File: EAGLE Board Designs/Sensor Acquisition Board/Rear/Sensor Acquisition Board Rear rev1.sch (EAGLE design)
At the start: 26 parts, among them J10 JUMPER_0603_, J4 CONNECTOR-SENSOR_NF_S_RA_BLACK, J5 CONNECTOR-SENSOR_NF_S_RA_BLACK, J6 CONNECTOR-SENSOR_NF_S_RA_BLACK, J7 CONNECTOR-SENSOR_NF_S_RA_BLACK, J9 CONNECTOR-CAN_NF_S_RA_BLACK, U1 VOLTAGE_REGULATOR_SOT-223_5V, U3 TCAN1051HQV-Q1

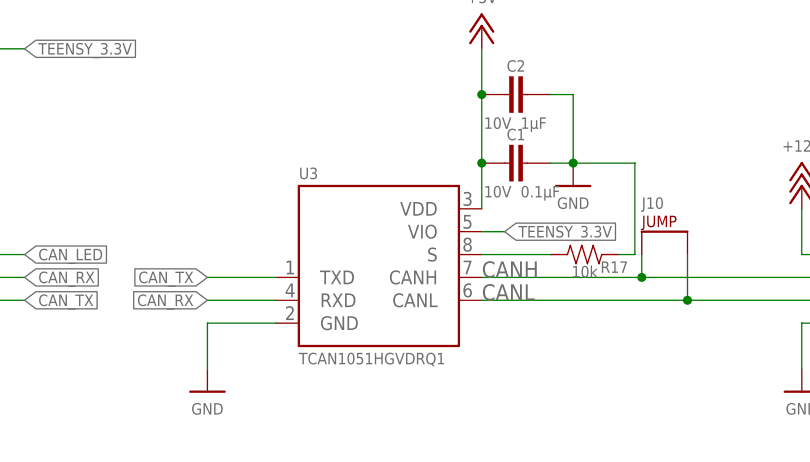
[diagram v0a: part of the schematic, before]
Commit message: TCAN to MCP on rear
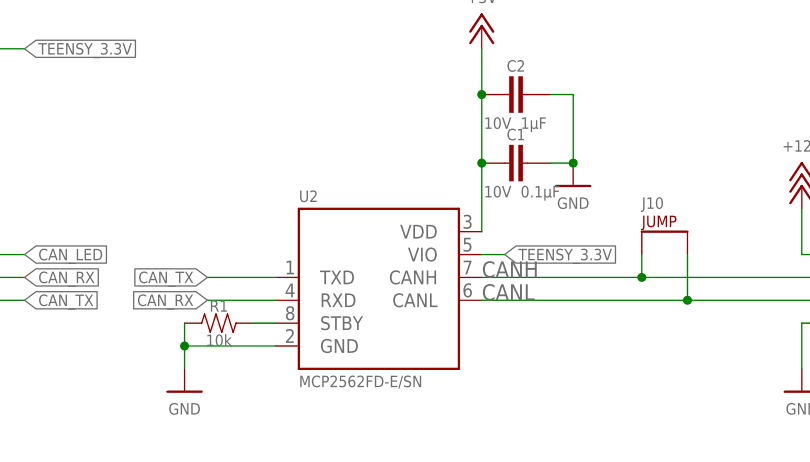
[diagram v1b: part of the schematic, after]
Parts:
- removed R17: RESISTOR_0603_10K, HyTechDevices:RESISTOR_0603_10K
- removed U3: TCAN1051HQV-Q1, HyTechDevices:TCAN1051HQV-Q1
- added R1: RESISTOR_0603_10K, HyTechDevices:RESISTOR_0603_10K
- added U2: MCP2562FD, HyTechDevices:MCP2562FD
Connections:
- removed net N$4: R17.1, U3.S
- new net N$3: R1.2, U2.STBY
- net +5V: now also U2.VDD; no longer U3.VDD
- net CANH: now also U2.CANH; no longer U3.CANH
- net CANL: now also U2.CANL; no longer U3.CANL
- net CAN_RX: now also U2.RXD; no longer U3.RXD
- net CAN_TX: now also U2.TXD; no longer U3.TXD
- net GND: now also R1.1, U2.GND; no longer R17.2, U3.GND
- net TEENSY_3.3V: now also U2.VIO; no longer U3.VIO
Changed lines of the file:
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@@
 <part name="P1" library="HyTechSupplies" deviceset="+5V" device=""/>
 <part name="P2" library="HyTechSupplies" deviceset="GND" device=""/>
-<part name="U3" library="HyTechDevices" deviceset="TCAN1051*V-Q1" device="" technology="HQ"/>
 <part name="C1" library="HyTechDevices" deviceset="CAPACITOR_?_*" device="0603" technology="10V_0.1UF"/>
 <part name="GND1" library="HyTechSupplies" deviceset="GND" device=""/>
@@
 <part name="P9" library="HyTechSupplies" deviceset="GND" device=""/>
 <part name="P10" library="HyTechSupplies" deviceset="+5V" device=""/>
-<part name="R17" library="HyTechDevices" deviceset="RESISTOR_?_*" device="0603" technology="10K"/>
 <part name="J6" library="HyTechDevices" deviceset="CONNECTOR-SENSOR_?_*" device="NF_S_RA" technology="BLACK"/>
 <part name="J5" library="HyTechDevices" deviceset="CONNECTOR-SENSOR_?_*" device="NF_S_RA" technology="BLACK"/>
@@
 <part name="R14" library="HyTechDevices" deviceset="RESISTOR_?_*" device="0603" technology="12K" value="RESISTOR_0603_12K"/>
 <part name="A2" library="HyTechDevices" deviceset="TEENSY_4.0" device=""/>
+<part name="U2" library="HyTechDevices" deviceset="MCP2562FD" device=""/>
+<part name="R1" library="HyTechDevices" deviceset="RESISTOR_?_*" device="0603" technology="10K"/>
 </parts>
 <sheets>
@@
 <attribute name="VALUE" x="114.3" y="95.25" size="1.27" layer="96" align="top-center"/>
 </instance>
-<instance part="U3" gate="G$1" x="182.88" y="121.92" smashed="yes">
-<attribute name="NAME" x="182.88" y="122.682" size="1.27" layer="95"/>
-<attribute name="MPN" x="182.88" y="103.378" size="1.27" layer="95" align="top-left"/>
-</instance>
 <instance part="C1" gate="G$1" x="208.28" y="124.46" smashed="yes">
 <attribute name="NAME" x="207.01" y="127" size="1.27" layer="95" align="bottom-center"/>
@@
 <attribute name="CAPACITANCE" x="207.518" y="129.54" size="1.27" layer="96" align="top-left"/>
 </instance>
-<instance part="P3" gate="1" x="172.72" y="99.06" smashed="yes">
-<attribute name="VALUE" x="172.72" y="97.79" size="1.27" layer="96" align="top-center"/>
+<instance part="P3" gate="1" x="170.18" y="99.06" smashed="yes">
+<attribute name="VALUE" x="170.18" y="97.79" size="1.27" layer="96" align="top-center"/>
 </instance>
 <instance part="J9" gate="G$1" x="254" y="116.84" smashed="yes" rot="MR0">
@@
 <attribute name="VALUE" x="43.18" y="129.54" size="1.27" layer="96" align="bottom-center"/>
 </instance>
-<instance part="R17" gate="G$1" x="215.9" y="114.3" smashed="yes">
-<attribute name="NAME" x="217.932" y="112.268" size="1.27" layer="95" align="bottom-center"/>
-<attribute name="RESISTANCE" x="214.63" y="113.03" size="1.27" layer="96" align="top-center"/>
-</instance>
 <instance part="J6" gate="G$1" x="215.9" y="200.66" smashed="yes" rot="MR0">
 <attribute name="NAME" x="215.9" y="201.295" size="1.27" layer="95" rot="MR0"/>
@@
 </instance>
 <instance part="A2" gate="G$1" x="121.92" y="144.78" smashed="yes"/>
+<instance part="U2" gate="G$1" x="182.88" y="119.38" smashed="yes">
+<attribute name="NAME" x="182.88" y="120.142" size="1.27" layer="95"/>
+<attribute name="MPN" x="182.88" y="100.838" size="1.27" layer="95" align="top-left"/>
+</instance>
+<instance part="R1" gate="G$1" x="175.26" y="106.68" smashed="yes">
+<attribute name="NAME" x="173.99" y="107.95" size="1.27" layer="95" align="bottom-center"/>
+<attribute name="RESISTANCE" x="173.99" y="105.41" size="1.27" layer="96" align="top-center"/>
+</instance>
 </instances>
 <busses>
@@
 <wire x1="213.36" y1="132.08" x2="213.36" y2="124.46" width="0.1524" layer="91"/>
 <junction x="213.36" y="124.46"/>
-<wire x1="213.36" y1="124.46" x2="220.218" y2="124.46" width="0.1524" layer="91"/>
-<pinref part="R17" gate="G$1" pin="2"/>
-<wire x1="218.44" y1="114.3" x2="220.218" y2="114.3" width="0.1524" layer="91"/>
-<wire x1="220.218" y1="114.3" x2="220.218" y2="124.46" width="0.1524" layer="91"/>
-</segment>
-<segment>
-<pinref part="U3" gate="G$1" pin="GND"/>
-<wire x1="180.34" y1="106.68" x2="172.72" y2="106.68" width="0.1524" layer="91"/>
-<wire x1="172.72" y1="106.68" x2="172.72" y2="101.6" width="0.1524" layer="91"/>
-<pinref part="P3" gate="1" pin="GND"/>
 </segment>
 <segment>
@@
 <junction x="109.22" y="190.5"/>
 </segment>
+<segment>
+<pinref part="U2" gate="G$1" pin="GND"/>
+<wire x1="180.34" y1="104.14" x2="170.18" y2="104.14" width="0.1524" layer="91"/>
+<pinref part="R1" gate="G$1" pin="1"/>
+<wire x1="170.18" y1="106.68" x2="170.18" y2="104.14" width="0.1524" layer="91"/>
+<pinref part="P3" gate="1" pin="GND"/>
+<wire x1="170.18" y1="104.14" x2="170.18" y2="101.6" width="0.1524" layer="91"/>
+<junction x="170.18" y="104.14"/>
+</segment>
 </net>
 <net name="+5V" class="0">
@@
 <segment>
 <pinref part="C1" gate="G$1" pin="2"/>
-<wire x1="203.2" y1="119.38" x2="203.2" y2="124.46" width="0.1524" layer="91"/>
+<wire x1="203.2" y1="116.84" x2="203.2" y2="124.46" width="0.1524" layer="91"/>
 <wire x1="203.2" y1="124.46" x2="203.2" y2="132.08" width="0.1524" layer="91"/>
 <junction x="203.2" y="124.46"/>
@@
 <wire x1="203.2" y1="132.08" x2="203.2" y2="137.16" width="0.1524" layer="91"/>
 <junction x="203.2" y="132.08"/>
-<pinref part="U3" gate="G$1" pin="VDD"/>
+<pinref part="U2" gate="G$1" pin="VDD"/>
 </segment>
 <segment>
@@
 <net name="CANH" class="0">
 <segment>
-<pinref part="U3" gate="G$1" pin="CANH"/>
 <pinref part="J9" gate="G$1" pin="CANH"/>
 <label x="203.2" y="111.76" size="1.778" layer="95"/>
@@
 <wire x1="220.98" y1="114.3" x2="220.98" y2="111.76" width="0.1524" layer="91"/>
 <junction x="220.98" y="111.76"/>
+<pinref part="U2" gate="G$1" pin="CANH"/>
 </segment>
 </net>
 <net name="CANL" class="0">
 <segment>
-<pinref part="U3" gate="G$1" pin="CANL"/>
 <pinref part="J9" gate="G$1" pin="CANL"/>
 <wire x1="203.2" y1="109.22" x2="226.06" y2="109.22" width="0.1524" layer="91"/>
@@
 <wire x1="226.06" y1="114.3" x2="226.06" y2="109.22" width="0.1524" layer="91"/>
 <junction x="226.06" y="109.22"/>
+<pinref part="U2" gate="G$1" pin="CANL"/>
 </segment>
 </net>
@@
 </segment>
 </net>
-<net name="N$4" class="0">
-<segment>
-<pinref part="U3" gate="G$1" pin="S"/>
-<pinref part="R17" gate="G$1" pin="1"/>
-<wire x1="203.2" y1="114.3" x2="210.82" y2="114.3" width="0.1524" layer="91"/>
-</segment>
-</net>
 <net name="TEENSY_3.3V" class="0">
 <segment>
@@
 </segment>
 <segment>
-<pinref part="U3" gate="G$1" pin="VIO"/>
-<wire x1="203.2" y1="116.84" x2="205.74" y2="116.84" width="0.1524" layer="91"/>
-<label x="205.74" y="116.84" size="1.27" layer="95" xref="yes"/>
+<label x="205.74" y="114.3" size="1.27" layer="95" xref="yes"/>
+<pinref part="U2" gate="G$1" pin="VIO"/>
+<wire x1="203.2" y1="114.3" x2="205.74" y2="114.3" width="0.1524" layer="91"/>
 </segment>
 </net>
@@
 </segment>
 <segment>
-<pinref part="U3" gate="G$1" pin="RXD"/>
 <wire x1="180.34" y1="109.22" x2="172.72" y2="109.22" width="0.1524" layer="91"/>
 <label x="172.72" y="109.22" size="1.27" layer="95" rot="MR0" xref="yes"/>
+<pinref part="U2" gate="G$1" pin="RXD"/>
 </segment>
 </net>
@@
 </segment>
 <segment>
-<pinref part="U3" gate="G$1" pin="TXD"/>
 <wire x1="180.34" y1="111.76" x2="172.72" y2="111.76" width="0.1524" layer="91"/>
 <label x="172.72" y="111.76" size="1.27" layer="95" rot="MR0" xref="yes"/>
-</segment>
-</net>
+<pinref part="U2" gate="G$1" pin="TXD"/>
+</segment>
+</net>
+<net name="N$3" class="0">
+<segment>
+<pinref part="U2" gate="G$1" pin="STBY"/>
+<pinref part="R1" gate="G$1" pin="2"/>
+<wire x1="180.34" y1="106.68" x2="177.8" y2="106.68" width="0.1524" layer="91"/>
+</segment>
+</net>

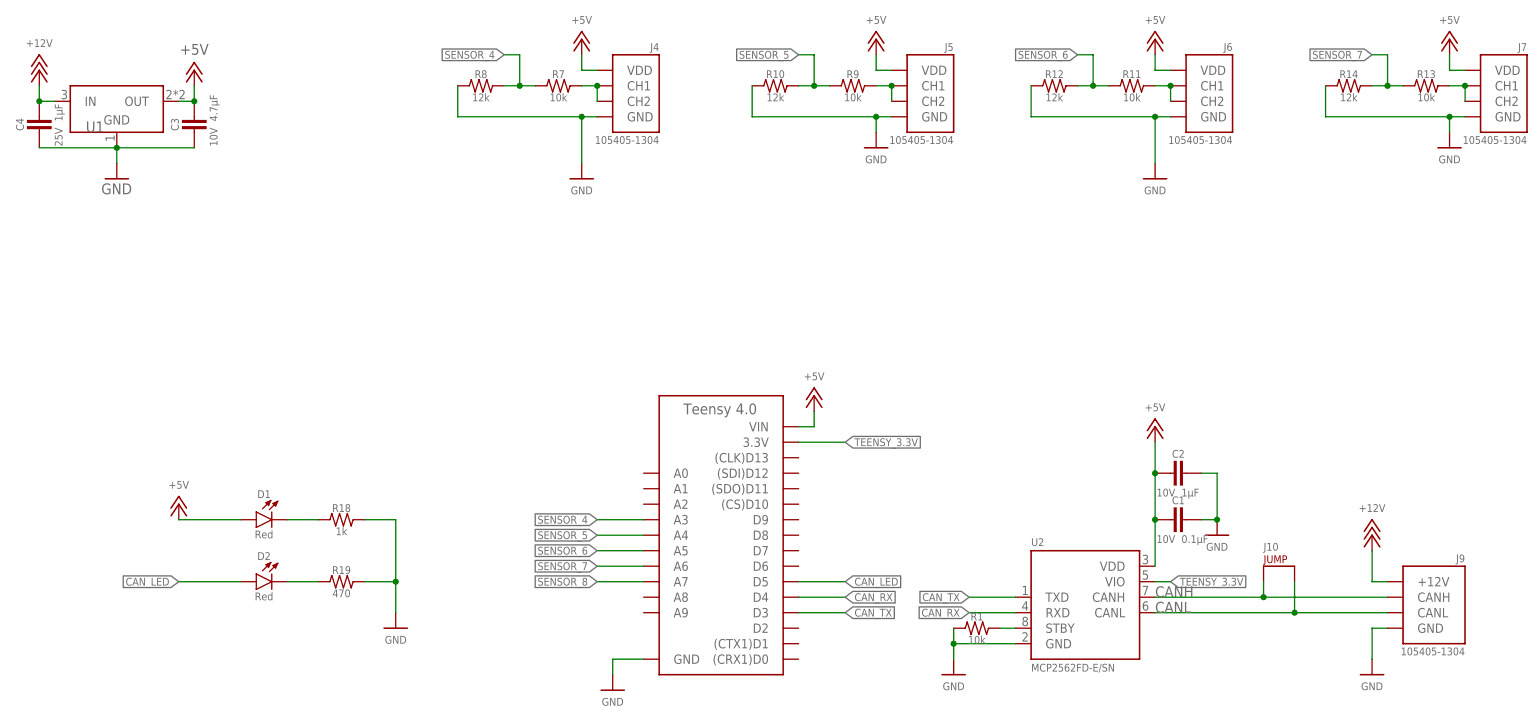
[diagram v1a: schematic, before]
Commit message: Fixed solder mask
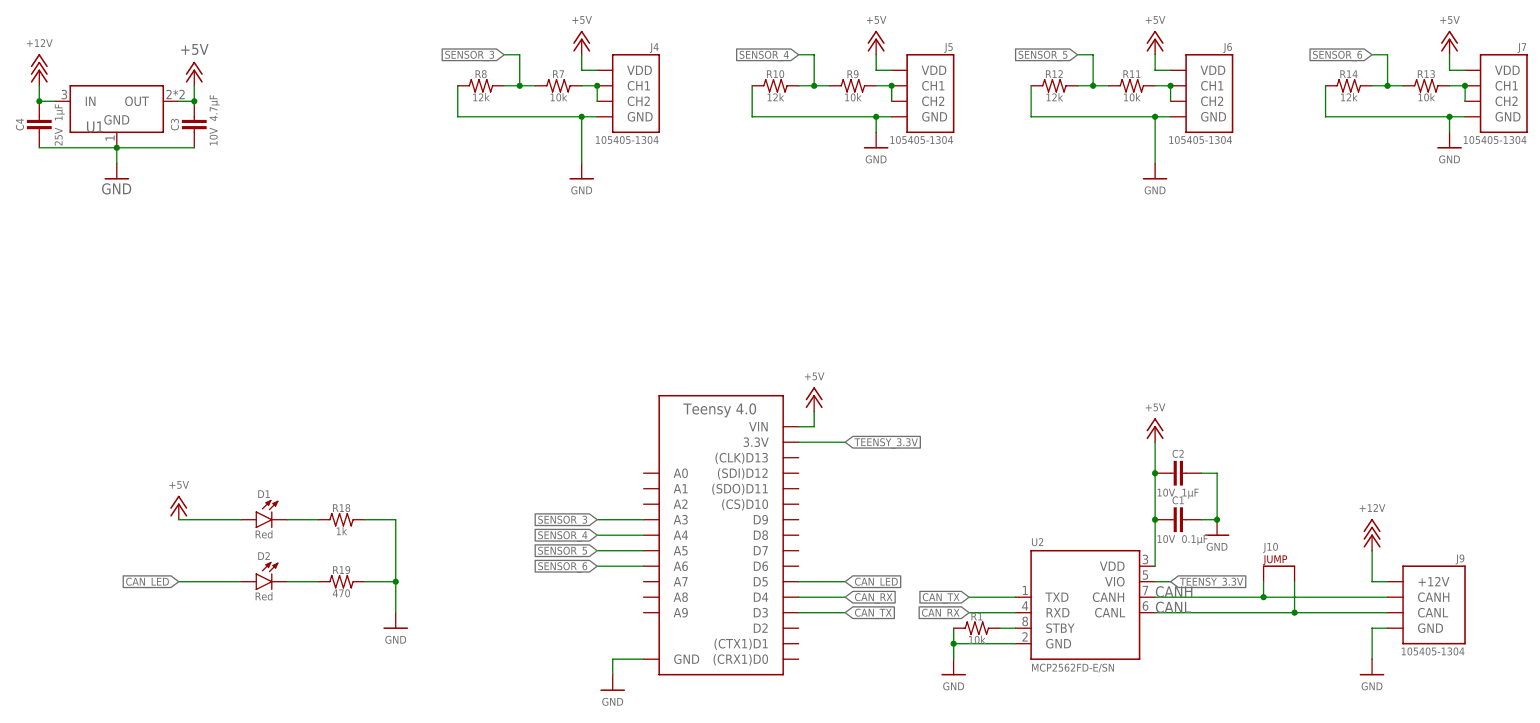
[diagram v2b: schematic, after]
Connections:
- removed net SENSOR_7: A2.A6, R13.1, R14.2
- removed net SENSOR_8: A2.A7
- new net SENSOR_3: A2.A3, R7.1, R8.2
- net SENSOR_4: now also A2.A4, R10.2, R9.1; no longer A2.A3, R7.1, R8.2
- net SENSOR_5: now also A2.A5, R11.1, R12.2; no longer A2.A4, R10.2, R9.1
- net SENSOR_6: now also A2.A6, R13.1, R14.2; no longer A2.A5, R11.1, R12.2
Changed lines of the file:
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@@
 </segment>
 </net>
-<net name="SENSOR_4" class="0">
+<net name="SENSOR_3" class="0">
 <segment>
 <wire x1="119.38" y1="124.46" x2="111.76" y2="124.46" width="0.1524" layer="91"/>
@@
 </segment>
 </net>
-<net name="SENSOR_5" class="0">
+<net name="SENSOR_4" class="0">
 <segment>
 <wire x1="119.38" y1="121.92" x2="111.76" y2="121.92" width="0.1524" layer="91"/>
@@
 </segment>
 </net>
-<net name="SENSOR_6" class="0">
+<net name="SENSOR_5" class="0">
 <segment>
 <wire x1="119.38" y1="119.38" x2="111.76" y2="119.38" width="0.1524" layer="91"/>
@@
 </segment>
 </net>
-<net name="SENSOR_7" class="0">
+<net name="SENSOR_6" class="0">
 <segment>
 <wire x1="119.38" y1="116.84" x2="111.76" y2="116.84" width="0.1524" layer="91"/>
@@
 </segment>
 </net>
-<net name="SENSOR_8" class="0">
-<segment>
-<wire x1="119.38" y1="114.3" x2="111.76" y2="114.3" width="0.1524" layer="91"/>
-<label x="111.76" y="114.3" size="1.27" layer="95" rot="MR0" xref="yes"/>
-<pinref part="A2" gate="G$1" pin="A7"/>
-</segment>
-</net>
